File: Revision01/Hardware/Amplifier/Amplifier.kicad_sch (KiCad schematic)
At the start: 12 parts, among them U1 INA333AIDGKR, U2 TLV9061SQDBVRQ1

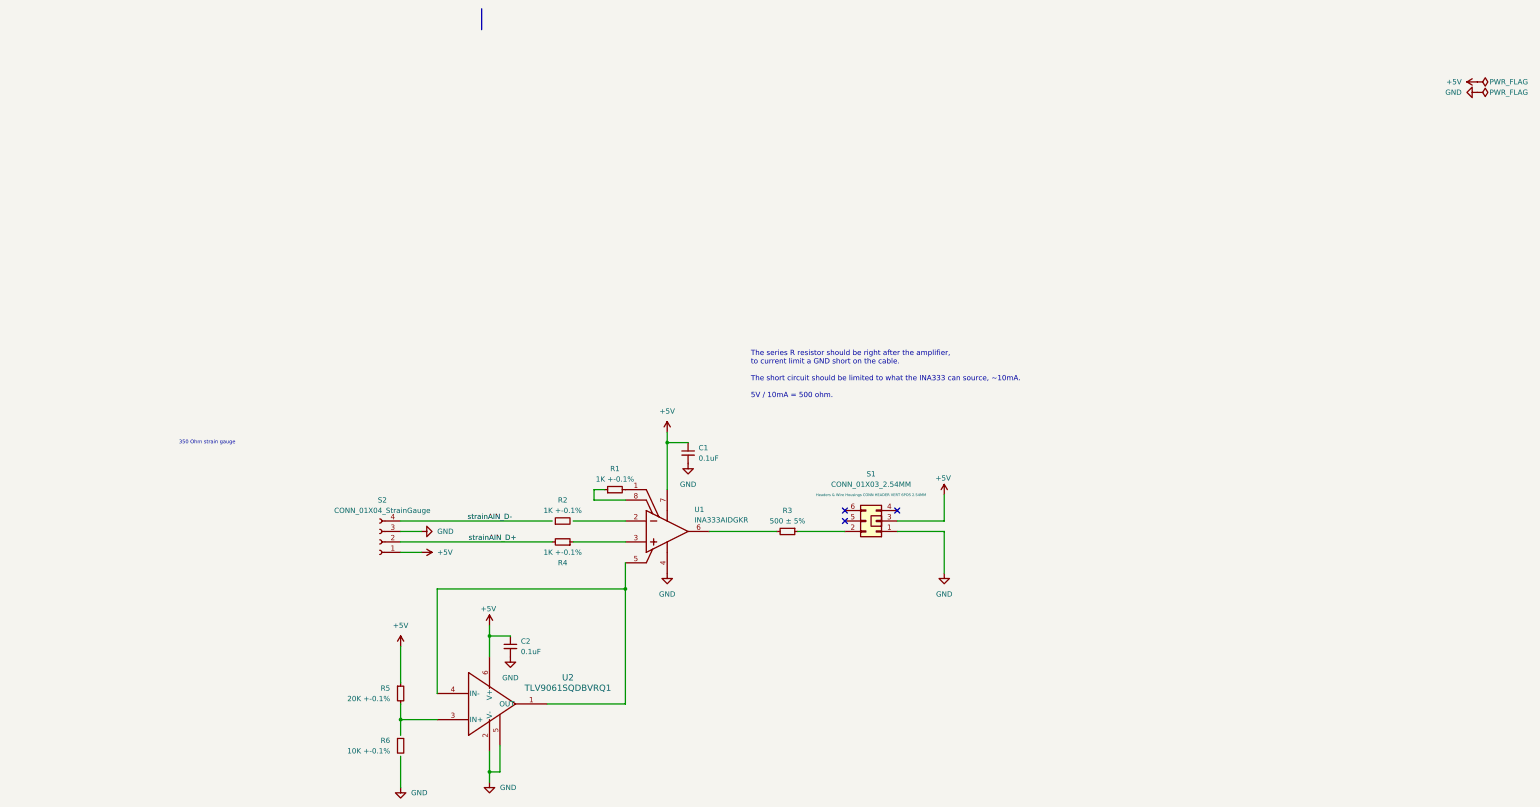
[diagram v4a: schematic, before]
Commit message: . Exported BOM (.csv), gerbers & dill files, 3D Model (.step) file to Product/2025-08-16 for both Amplifier & Hub boards.
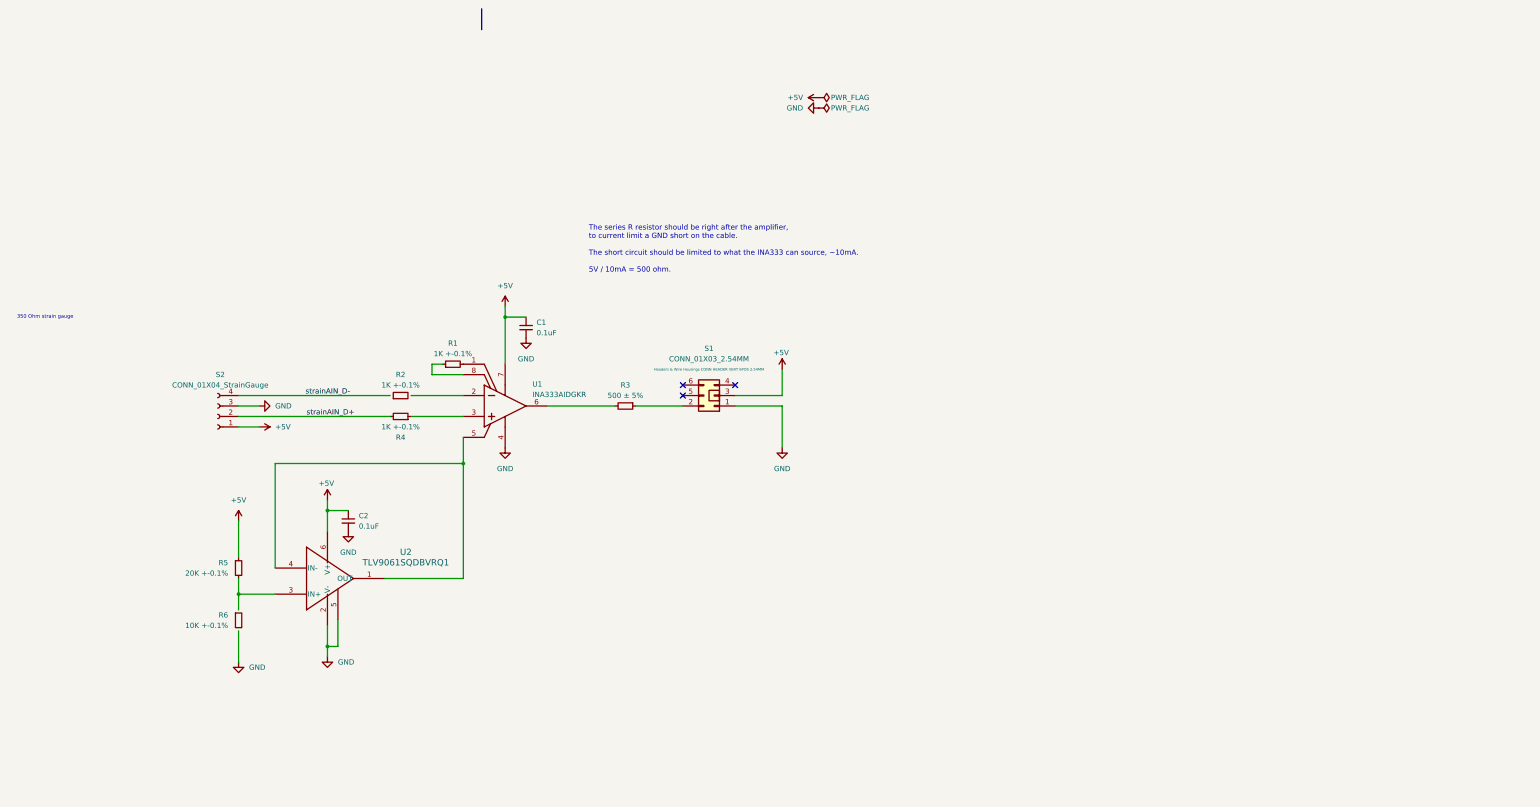
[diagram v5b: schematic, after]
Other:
- company: (none) -> BCIT Racing
- title: (none) -> Amplifier
- moved on the sheet: C1, C2, R1, R2, R3, R4, R5, R6, S1, S2, U1, U2

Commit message: . Made sure amplifier passive silk screen doesn't overlap pads . Added 6xAA battery holder to hub BOM . Exported gerbers, drl files .zip (PCBWay approved)
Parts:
- S1: now left out of the parts list
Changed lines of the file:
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@@
 		(unit 1)
 		(exclude_from_sim no)
-		(in_bom yes)
+		(in_bom no)
 		(on_board yes)
 		(dnp no)

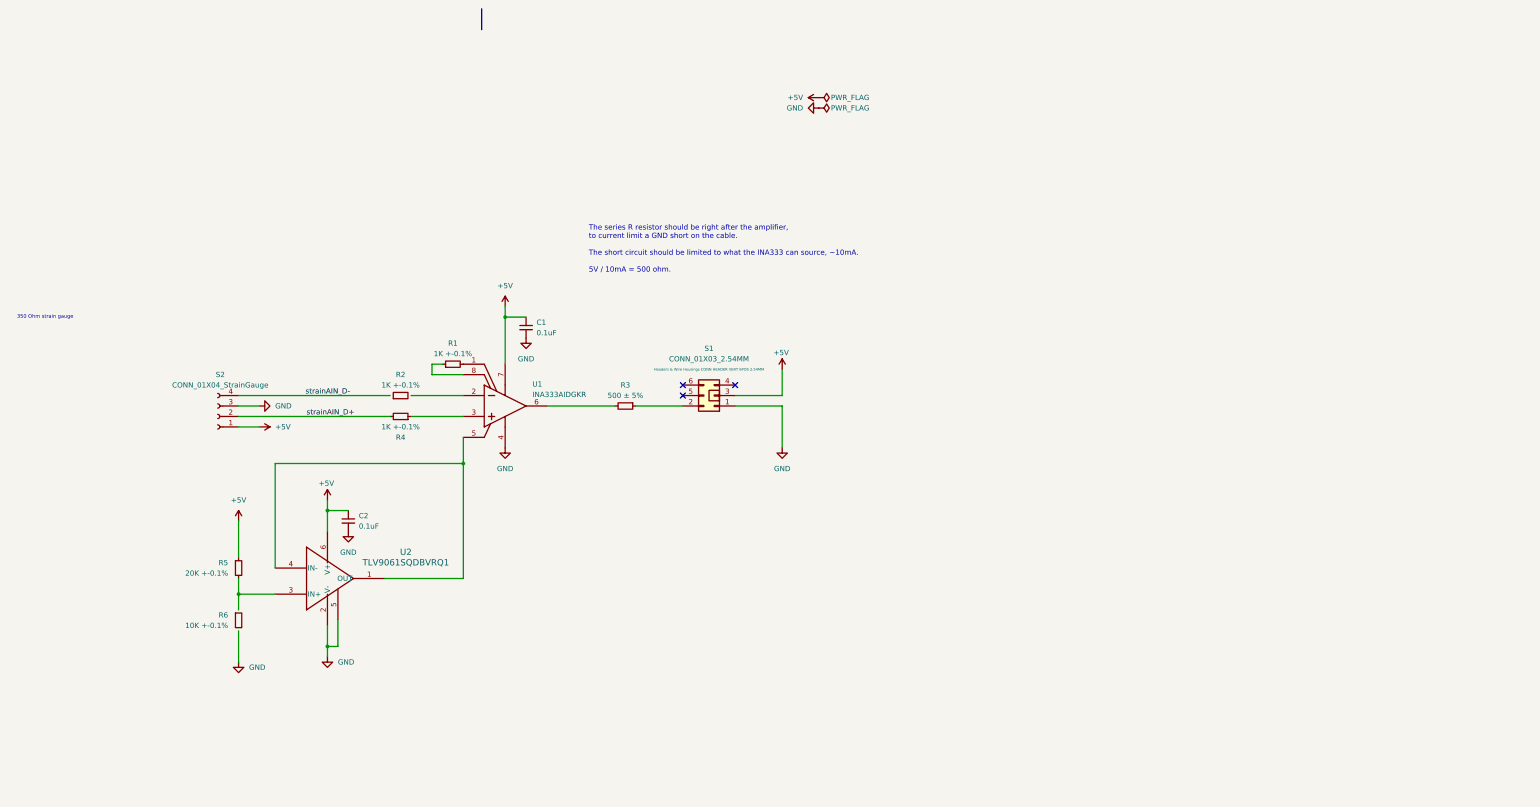
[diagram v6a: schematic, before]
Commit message: improved documentation and small cosmetic changes - buck bypass resistor has X to indicate it is optional - RC documentation on schematic updated - Considering affects of 5V rail not being 5V 	- Lowers strainAmplifier offset 	- reduces strainAnalog signal
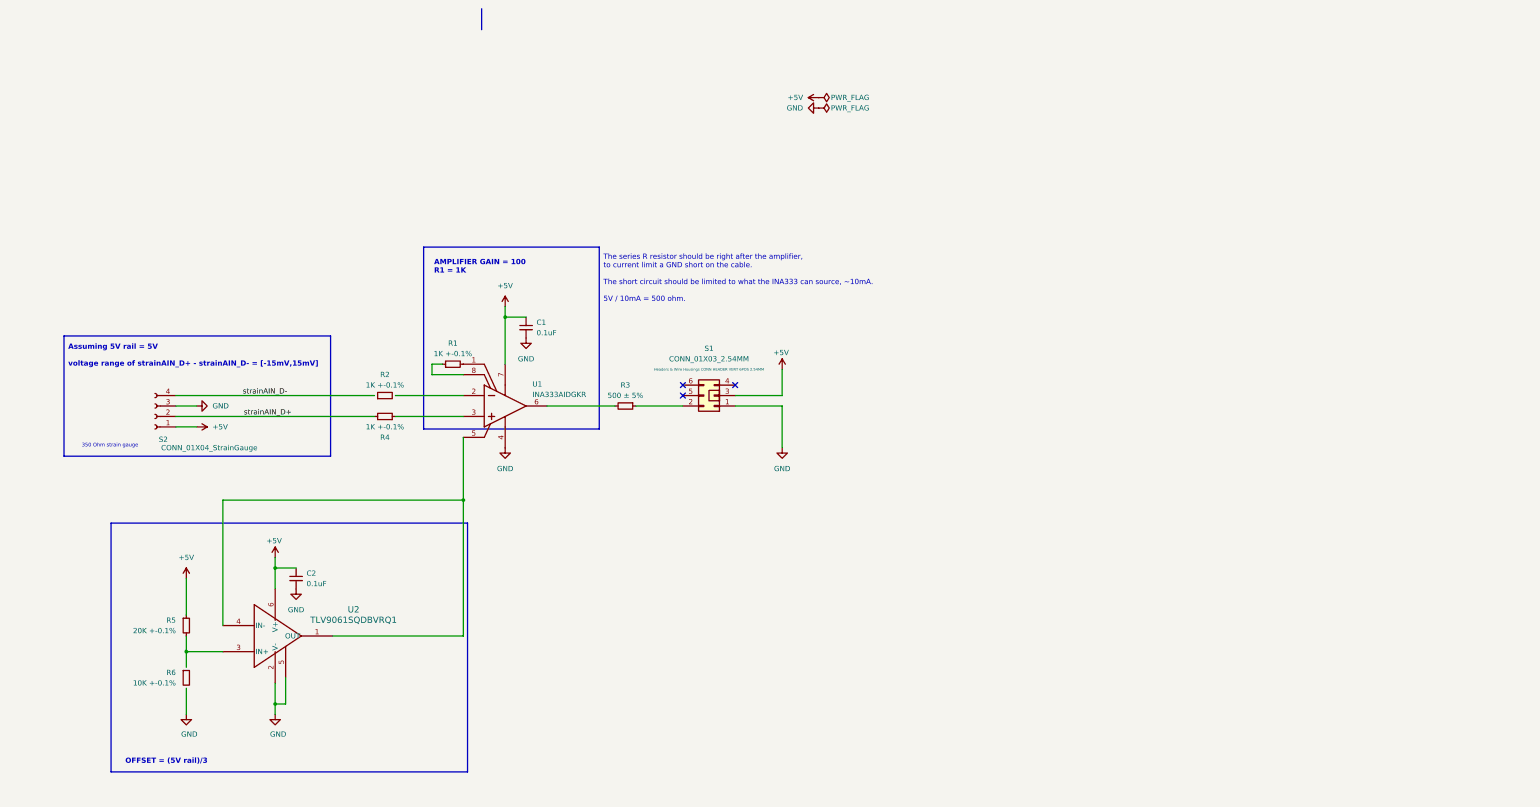
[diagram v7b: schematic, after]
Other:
- note added: "AMPLIFIER GAIN = 100 R1 = 1K"
- note added: "Assuming 5V rail = 5V voltage range of strainAIN_D+ - strainAIN_D- = [-15mV,15mV]"
- note added: "OFFSET = (5V rail)/3"
- moved on the sheet: C2, R2, R4, R5, R6, S2, U2

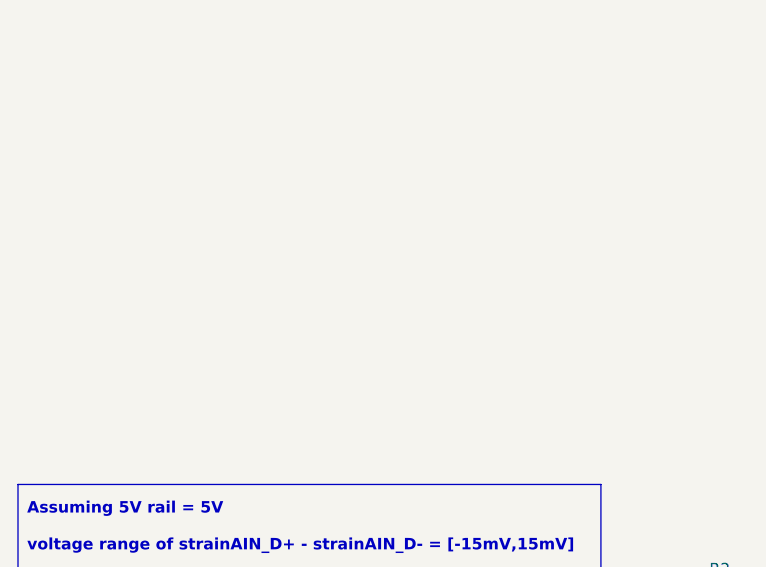
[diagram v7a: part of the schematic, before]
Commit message: changes to routing
-buck converter output capacitors placed at output of inductor
-output of buck-converter routed over to other layer to further avoid coupling between analog signals
-1M ohm resistors routed closer to analog signal( so it is less likely to become a victim)
-initial placement of stitching via's placed. With an average distance of 10mm between them
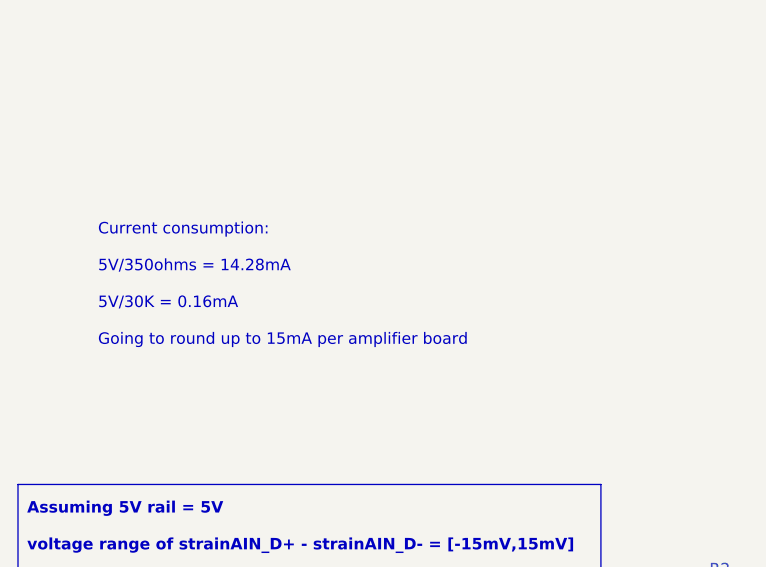
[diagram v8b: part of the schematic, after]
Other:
- note added: "Current consumption: 5V/350ohms = 14.28mA 5V/30K = 0.16mA Going to round up to 15mA per amplifier board"
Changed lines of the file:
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@@
+		)
+	)
+	(text "Current consumption:\n\n5V/350ohms = 14.28mA\n\n5V/30K = 0.16mA\n\nGoing to round up to 15mA per amplifier board\n"
+		(exclude_from_sim no)
+		(at 69.342 57.404 0)
+		(effects
+			(font
+				(size 1.27 1.27)
+			)
+			(justify left)
 		)
 	)
